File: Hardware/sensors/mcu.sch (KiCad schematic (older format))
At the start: 16 parts, among them SW301 reset, U301 AT25DF041A, U302 STM32F103R8, U303 8MHz

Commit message: splitted schematics are ready. MCU/Display board is ready.
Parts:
- R304: value R -> 100k
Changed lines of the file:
@@
-EESchema Schematic File Version 2  date Do 10 Mär 2011 03:25:53 CET
+EESchema Schematic File Version 2  date Do 10 Mär 2011 16:21:43 CET
 LIBS:power
 LIBS:device
@@
 EELAYER END
 $Descr A4 11700 8267
+encoding utf-8
 Sheet 3 8
 Title ""
@@
 P 6750 3700
 F 0 "R304" V 6830 3700 50  0000 C CNN
-F 1 "R" V 6750 3700 50  0000 C CNN
+F 1 "100k" V 6750 3700 50  0000 C CNN
 	1    6750 3700
 	0    -1   1    0

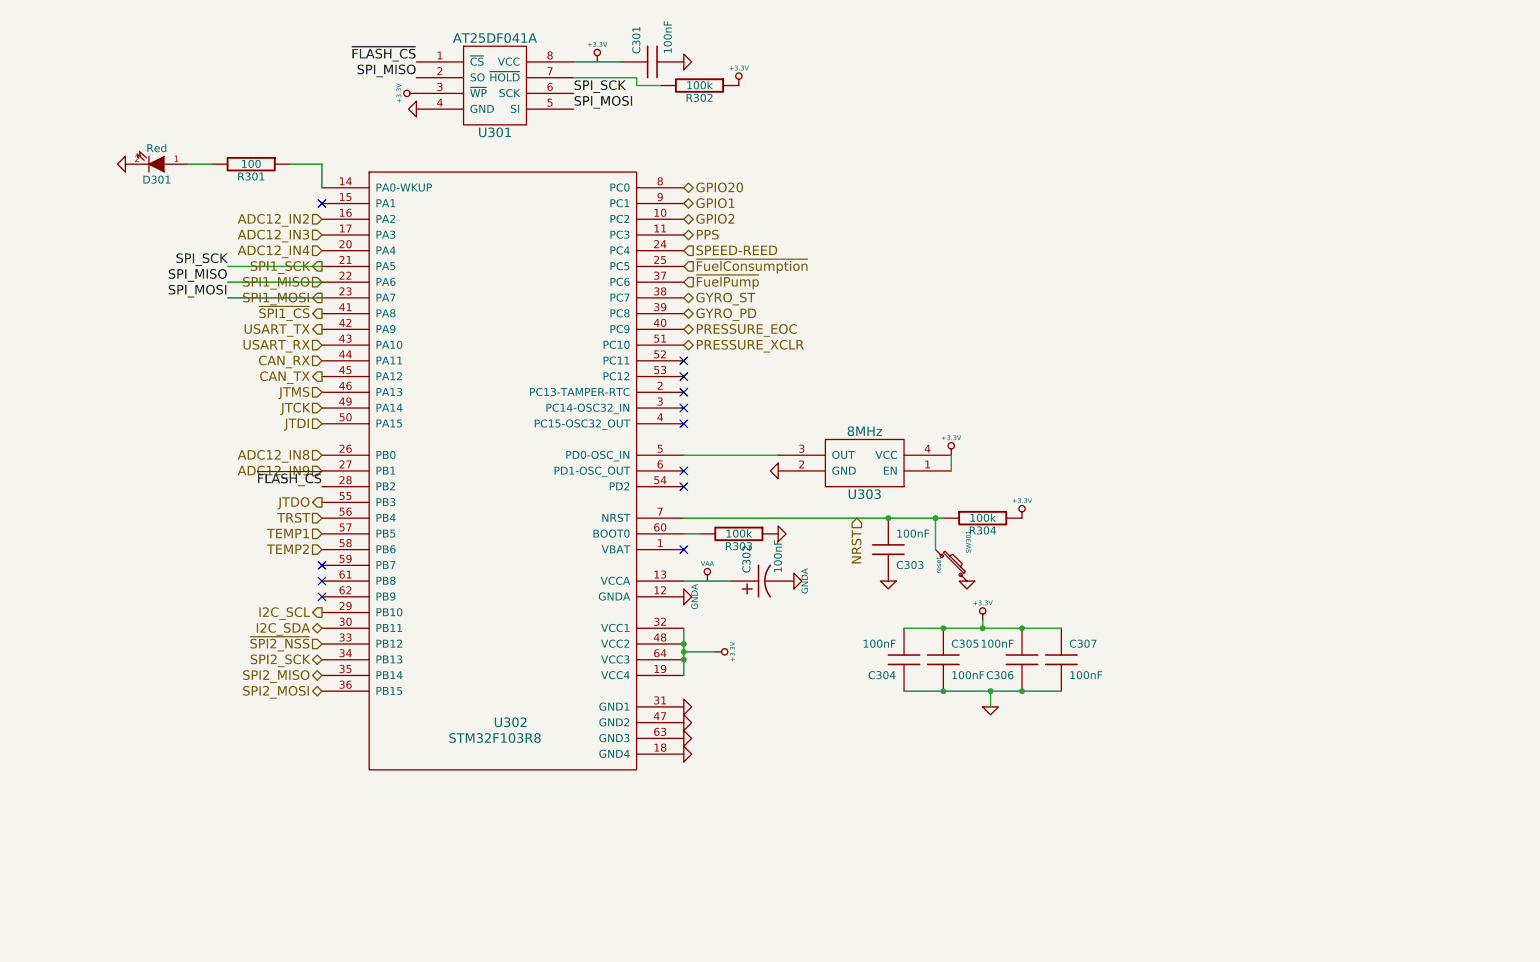
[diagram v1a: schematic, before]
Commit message: sensor board first version
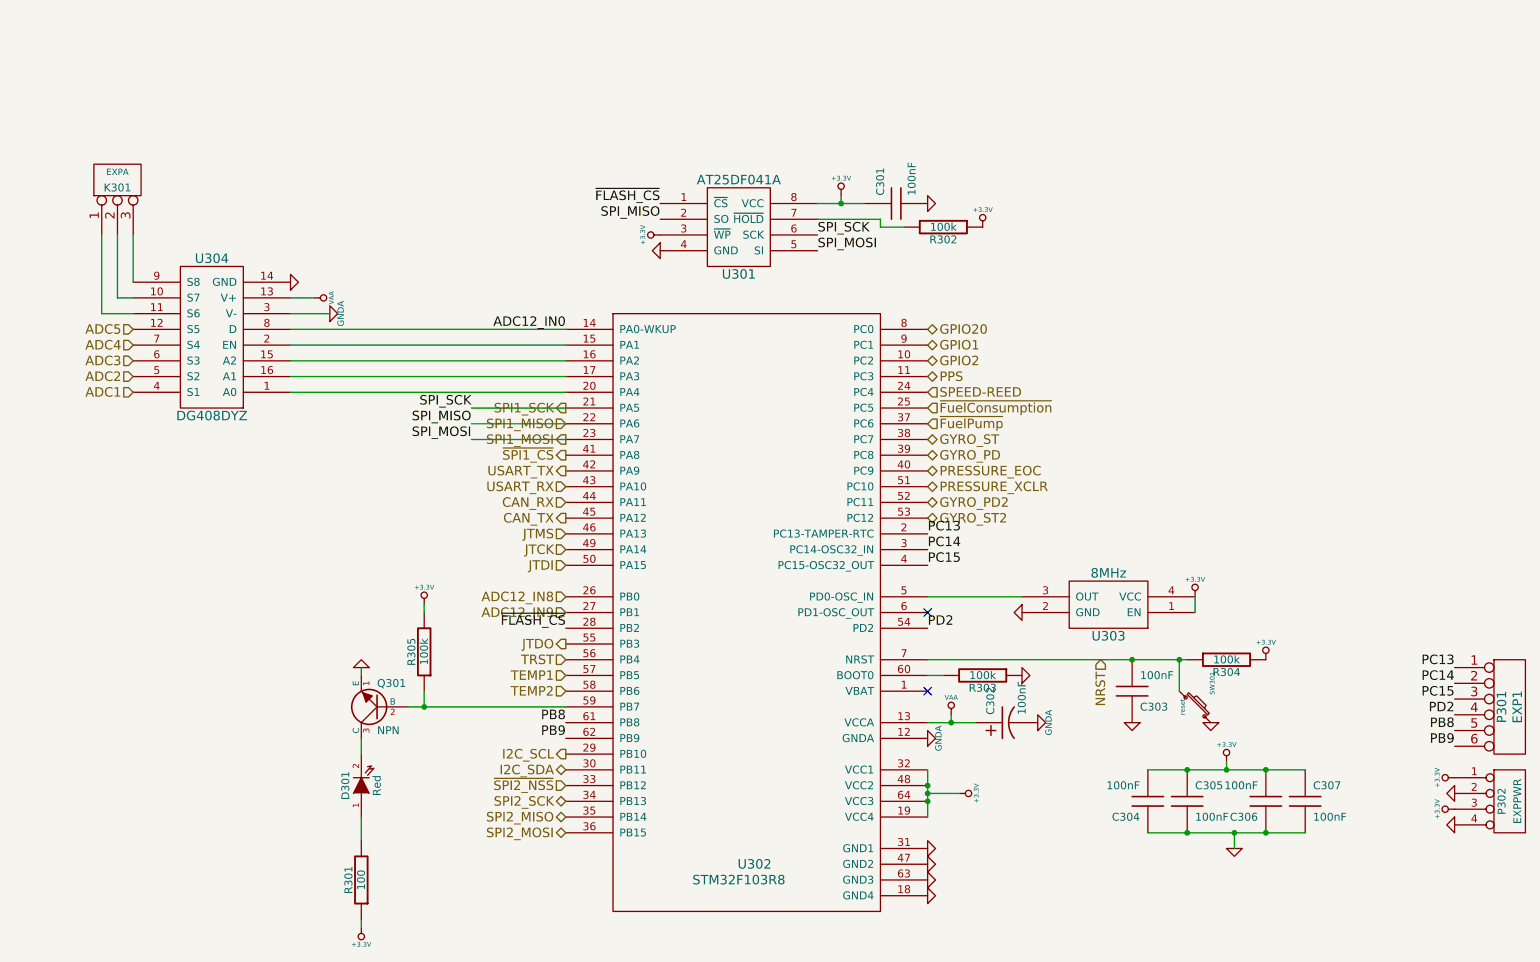
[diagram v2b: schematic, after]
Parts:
- added K301: EXPA, symbol CONN_3
- added P301: EXP1, symbol CONN_6
- added P302: EXPPWR, symbol CONN_4
- added Q301: NPN, symbol NPN
- added R305: 100k, symbol R
- added U304: DG408DYZ, symbol DG408
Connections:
- net +3.3V: now also C301.1, R301.1, U301.8 (VCC), P302.1 (P1), P302.3 (P3), R305.2
- net GND: now also P302.2 (P2), P302.4 (P4), Q301.1 (E), U304.14 (GND); no longer D301.2 (K)
- net GNDA: now also U304.3 (V-)
- net VAA: now also C302.1, U302.13 (VCCA), U304.13 (V+)
- net ADC12_IN0: now reaches U302.14 (PA0-WKUP)
- net ADC12_IN0: now also U304.8 (D); no longer R301.1
- net at U302.15 (PA1): now also U304.2 (EN)
- net PC13: now reaches U302.2 (PC13-TAMPER-RTC)
- net PC13: now also P301.1
- net PC14: now reaches U302.3 (PC14-OSC32_IN)
- net PC14: now also P301.2
- net PC15: now reaches U302.4 (PC15-OSC32_OUT)
- net PC15: now also P301.3
- net GYRO_PD2: now reaches U302.52 (PC11)
- net GYRO_ST2: now reaches U302.53 (PC12)
- net PD2: now reaches U302.54 (PD2)
- net PD2: now also P301.4
- net at U302.59 (PB7): now also Q301.2 (B), R305.1
- net PB8: now reaches U302.61 (PB8)
- net PB8: now also P301.5
- net PB9: now reaches U302.62 (PB9)
- net PB9: now also P301.6
- net ADC12_IN2: no longer names the net of U302.16 (PA2)
- net ADC12_IN2: now also U304.15 (A2)
- net ADC12_IN3: no longer names the net of U302.17 (PA3)
- net ADC12_IN3: now also U304.16 (A1)
- net ADC12_IN4: no longer names the net of U302.20 (PA4)
- net ADC12_IN4: now also U304.1 (A0)
- new net: D301.2 (K), Q301.3 (C)
- new net: K301.2 (PM), U304.10 (S7)
- new net: K301.1 (P1), U304.11 (S6)
- new net: K301.3 (P3), U304.9 (S8)
- new net ADC1: U304.4 (S1)
- new net ADC2: U304.5 (S2)
- new net ADC3: U304.6 (S3)
- new net ADC4: U304.7 (S4)
- new net ADC5: U304.12 (S5)
- no-connect marks 12 -> 2
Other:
- moved on the sheet: C301, C302, C303, C304, C305, C306, C307, D301, R301, R302, R303, R304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

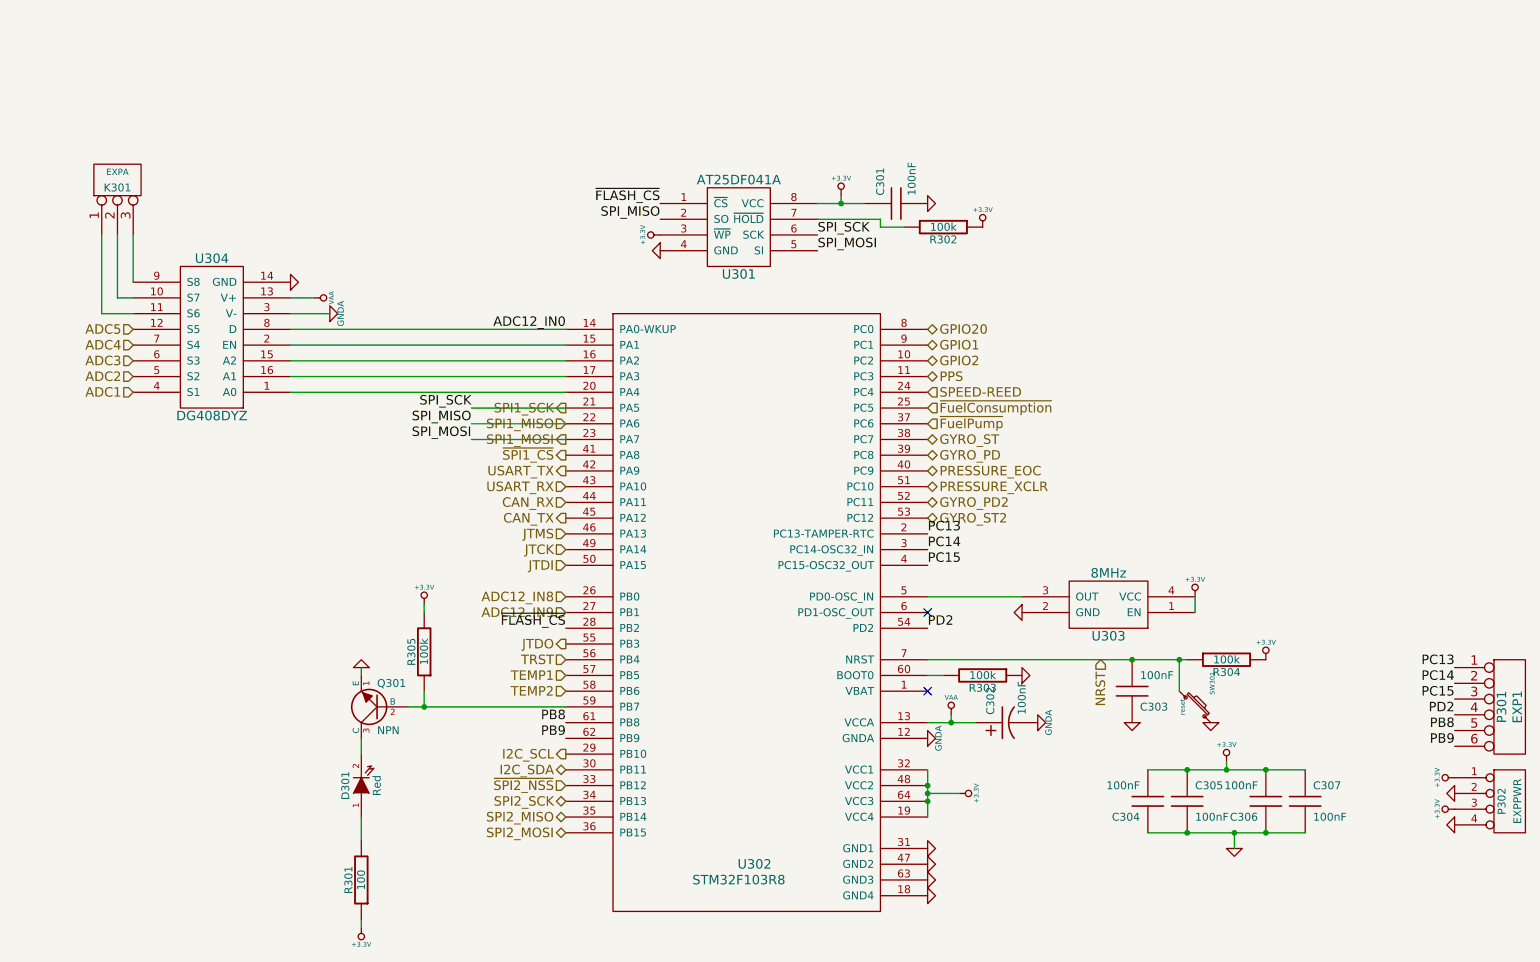
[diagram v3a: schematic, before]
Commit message: using adc instead of analog multiplexer for sensor board, some work on mcu board
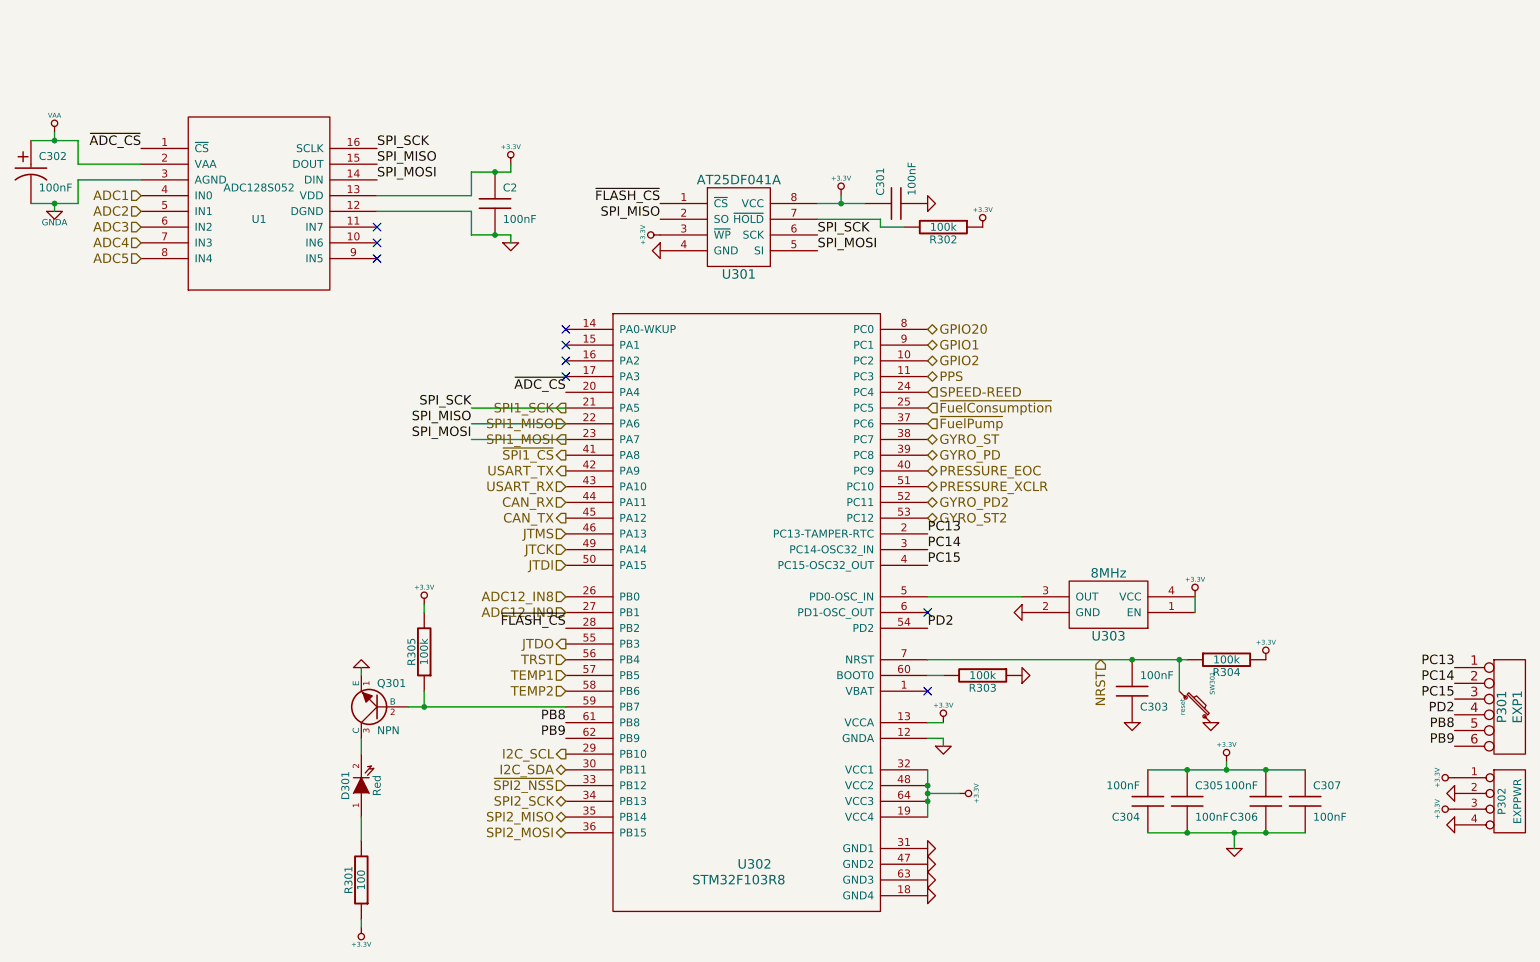
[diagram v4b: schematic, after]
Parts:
- removed K301: EXPA, symbol CONN_3
- removed U304: DG408DYZ, symbol DG408
- added C2: 100nF, symbol C
- added U1: ADC128S052, symbol ADC128S052
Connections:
- net +3.3V: now also U302.13 (VCCA), C2.1, U1.13 (VDD)
- net ADC1: now also U1.4 (IN0)
- net ADC2: now also U1.5 (IN1)
- net ADC3: now also U1.6 (IN2)
- net ADC4: now also U1.7 (IN3)
- net ADC5: now also U1.8 (IN4)
- net GND: now also U302.12 (GNDA), C2.2, U1.12 (DGND)
- net GNDA: now also U1.3 (AGND); no longer U302.12 (GNDA)
- net SPI1_MISO: now also U1.15 (DOUT)
- net SPI1_MOSI: now also U1.14 (DIN)
- net SPI1_SCK: now also U1.16 (SCLK)
- net VAA: now also U1.2 (VAA); no longer U302.13 (VCCA)
- net ~ADC_CS: now reaches U302.20 (PA4)
- net ~ADC_CS: now also U1.1 (~CS)
- net ADC12_IN0: no longer names the net of U302.14 (PA0-WKUP)
- no-connect marks 2 -> 9
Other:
- moved on the sheet: C302
